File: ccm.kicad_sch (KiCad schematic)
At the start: 22 parts, among them J1 Conn_01x04_Socket, J3 Conn_01x04_Socket, J4 Conn_01x04_Socket, J5 Conn_01x04_Socket, J6 Conn_01x02_Socket, J7 Conn_01x02_Socket, U1 Teensy4.1, U2 LM1117DT-1.8, U3 SN65HVD230, U4 SN65HVD230

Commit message: added DIP socket connector for teensy
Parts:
- U1: footprint teensy:Teensy41 -> teensy:CONN_4848-6000-CP_3MM
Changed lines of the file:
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@@
 			)
 		)
-		(property "Footprint" "teensy:Teensy41"
+		(property "Footprint" "teensy:CONN_4848-6000-CP_3MM"
 			(at 72.39 78.74 0)
 			(effects

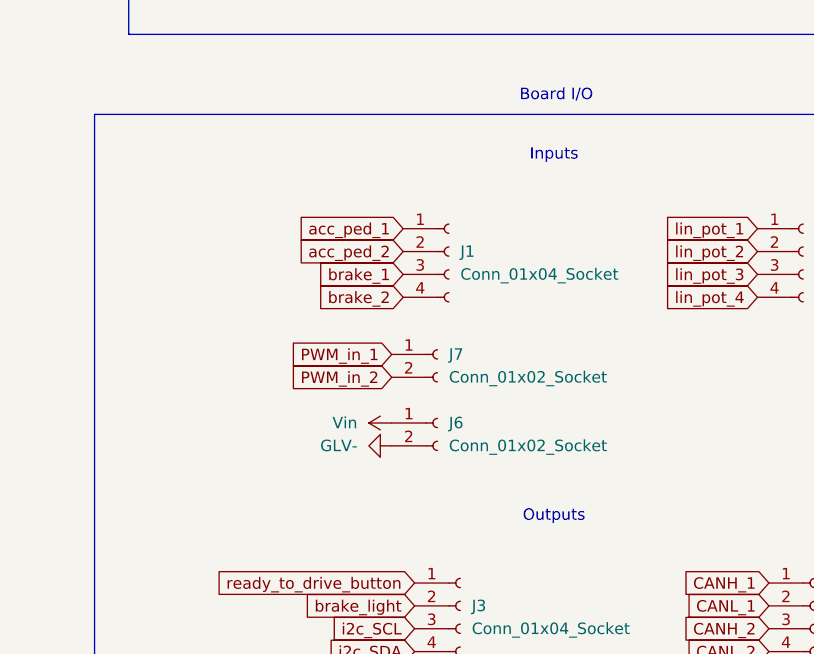
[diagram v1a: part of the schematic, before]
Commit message: change brake and accel connectors
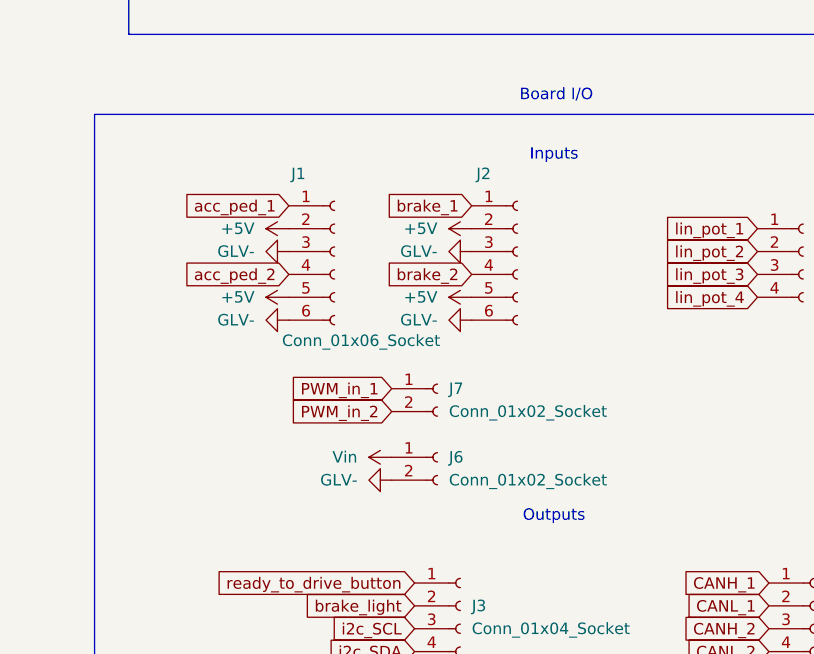
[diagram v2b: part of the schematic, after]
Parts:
- removed J1: Conn_01x04_Socket, Connector_Molex:Molex_Mini-Fit_Jr_5566-04A2_2x02_P4.20mm_Vertical, symbol Connector:Conn_01x04_Socket
- added J1, J2: Conn_01x06_Socket, Connector_Molex:Molex_Mini-Fit_Jr_5566-06A2_2x03_P4.20mm_Vertical, symbol Connector:Conn_01x06_Socket
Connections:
- net +5V: now also J1.2 (Pin_2), J1.5 (Pin_5), J2.2 (Pin_2), J2.5 (Pin_5)
- net GLV-: now also J1.3 (Pin_3), J1.6 (Pin_6), J2.3 (Pin_3), J2.6 (Pin_6)
- net acc_ped_1: now also J1.1 (Pin_1)
- net acc_ped_2: now also J1.4 (Pin_4)
- net brake_1: now also J2.1 (Pin_1)
- net brake_2: now also J2.4 (Pin_4)
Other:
- moved on the sheet: J6, J7

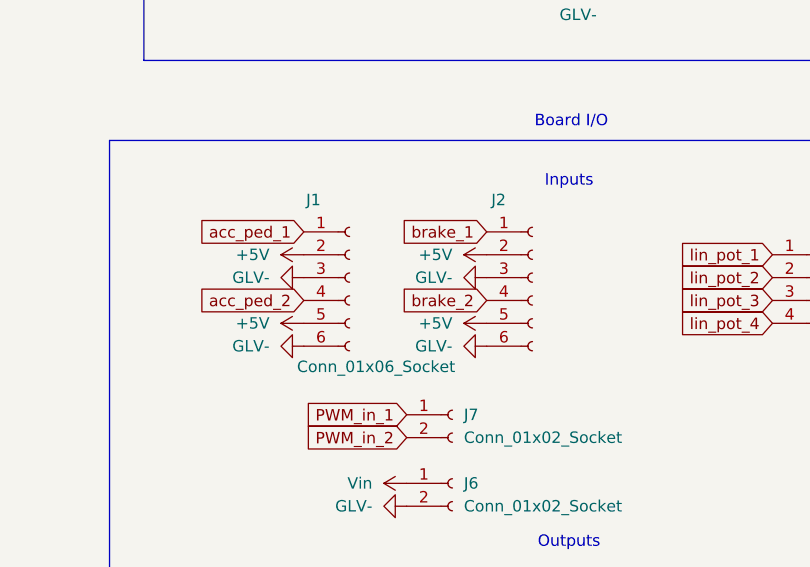
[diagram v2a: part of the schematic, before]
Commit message: remove 5v/glv from throttle/brake sensors
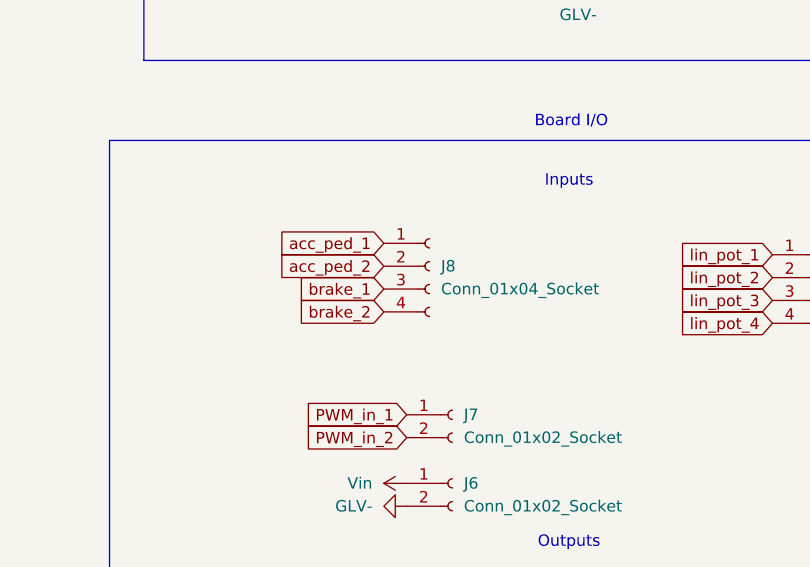
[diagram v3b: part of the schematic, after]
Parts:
- removed J1, J2: Conn_01x06_Socket, Connector_Molex:Molex_Mini-Fit_Jr_5566-06A2_2x03_P4.20mm_Vertical, symbol Connector:Conn_01x06_Socket
- added J8: Conn_01x04_Socket, Connector_Molex:Molex_Mini-Fit_Jr_5566-04A2_2x02_P4.20mm_Vertical, symbol Connector:Conn_01x04_Socket
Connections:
- net acc_ped_1: now also J8.1 (Pin_1)
- net acc_ped_2: now also J8.2 (Pin_2)
- net brake_1: now also J8.3 (Pin_3)
- net brake_2: now also J8.4 (Pin_4)

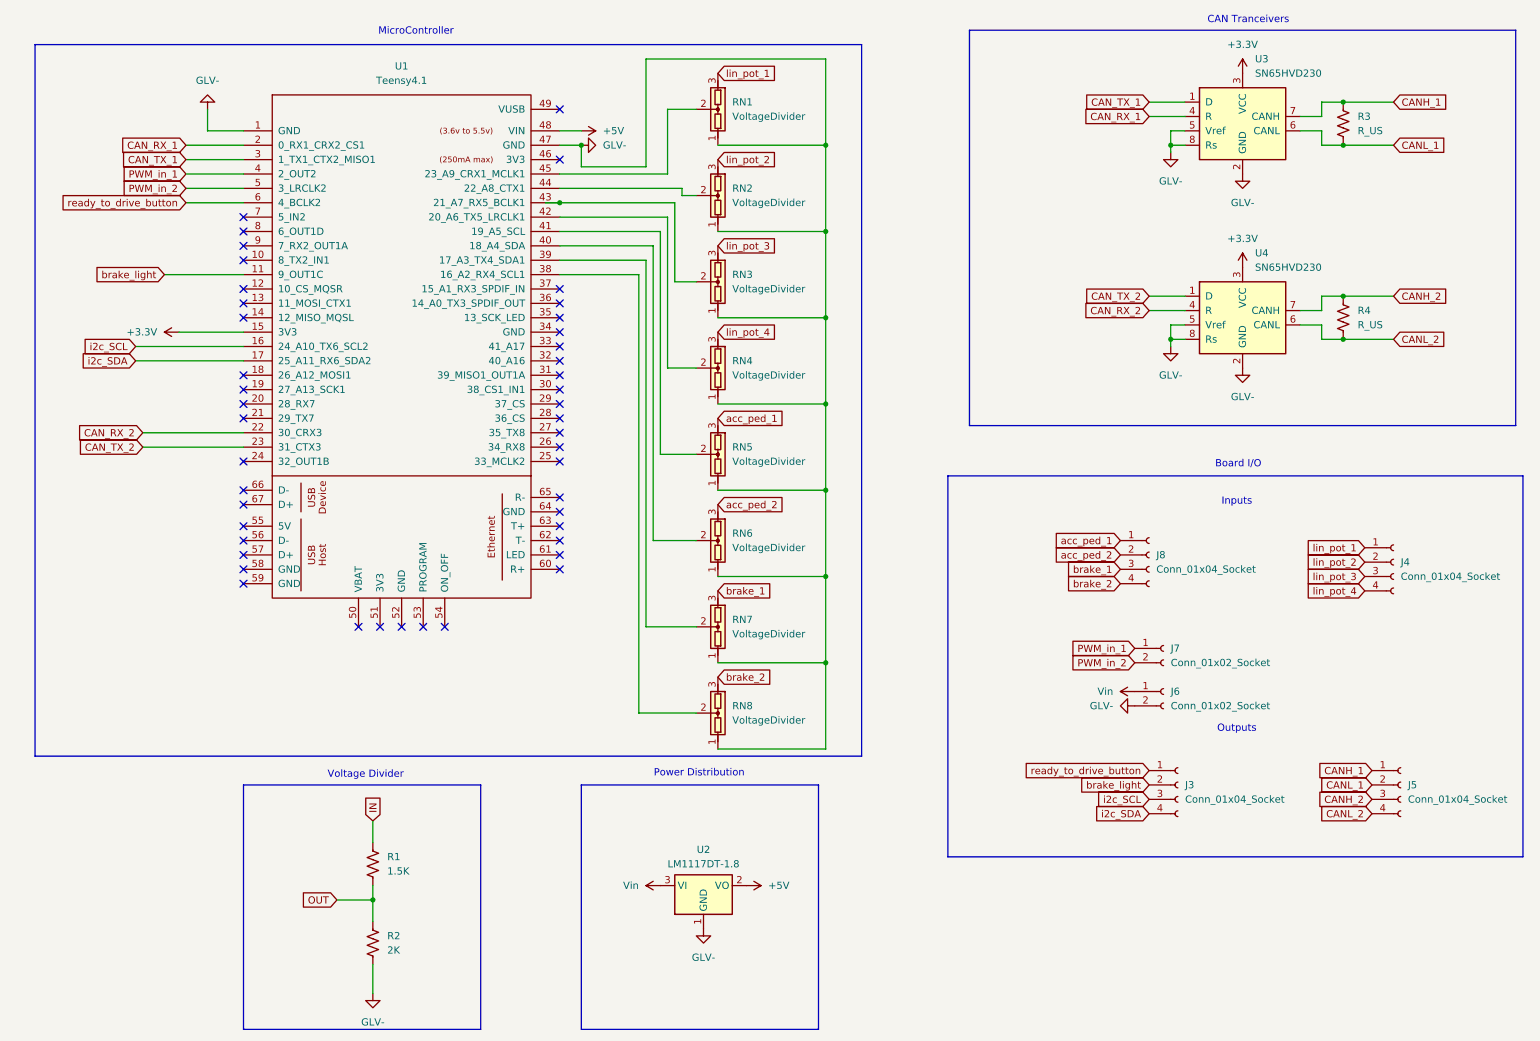
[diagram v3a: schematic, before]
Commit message: add mosfet for brake light output and decoupling capacitors
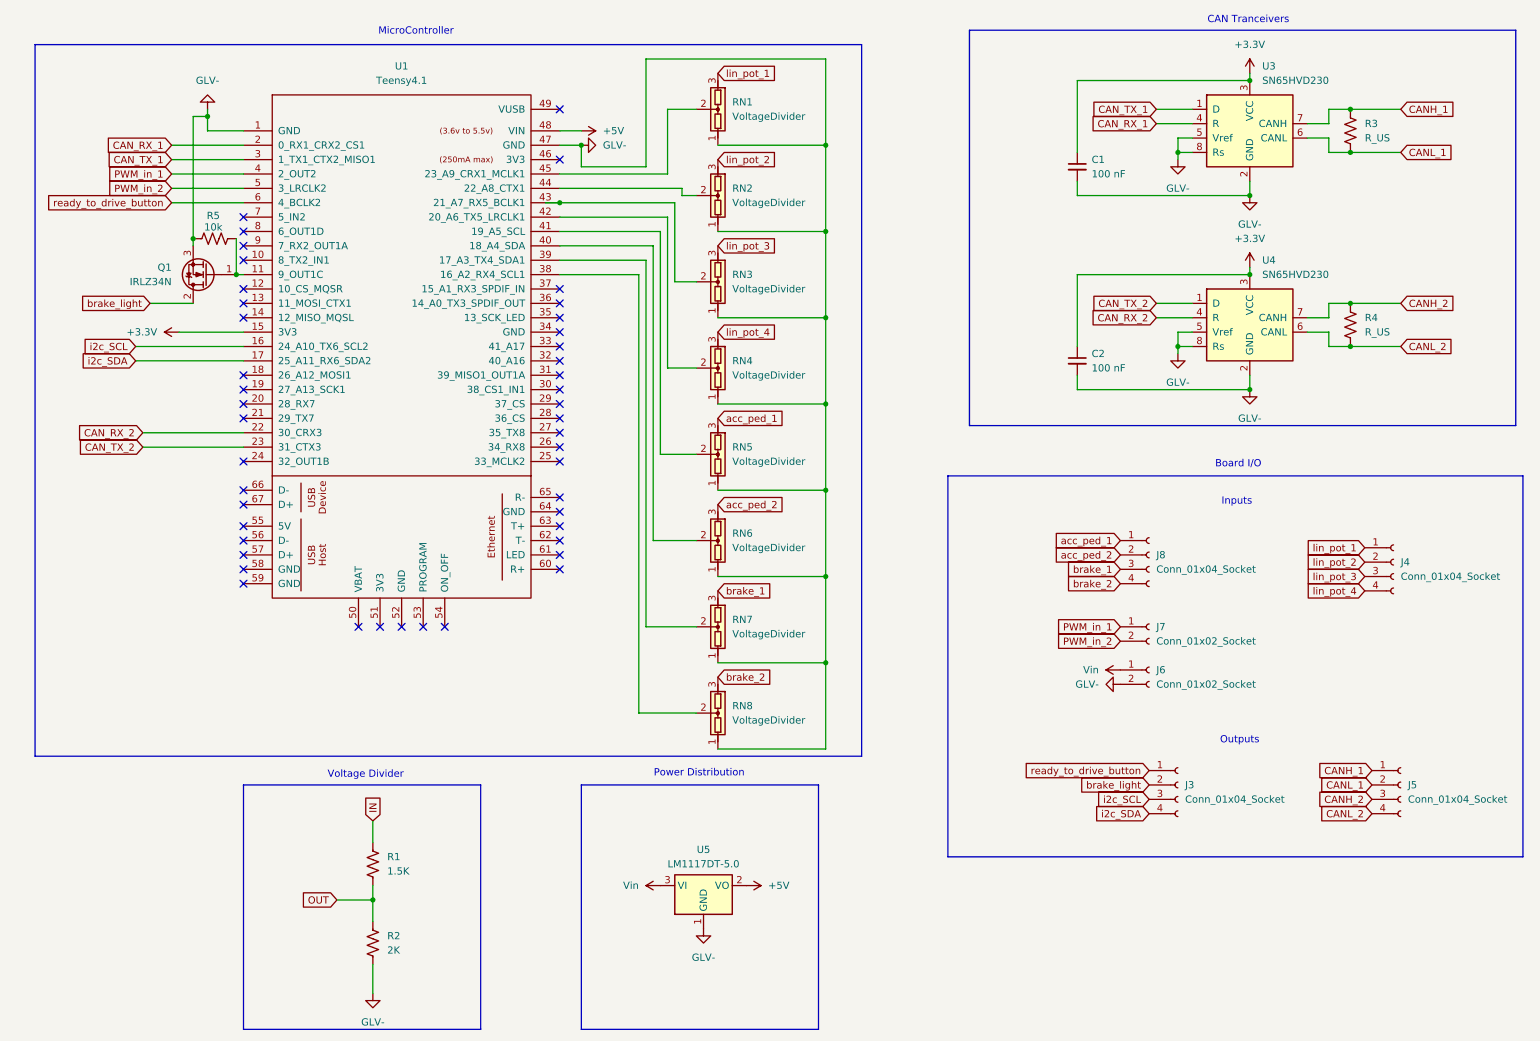
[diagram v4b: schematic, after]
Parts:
- removed U2: LM1117DT-1.8, Package_TO_SOT_SMD:TO-252-3_TabPin2, symbol Regulator_Linear:LM1117DT-1.8
- added C1, C2: 100 nF, Capacitor_SMD:C_0805_2012Metric_Pad1.18x1.45mm_HandSolder, symbol Device:C_Small
- added Q1: IRLZ34N, Package_TO_SOT_THT:TO-220-3_Vertical, symbol Transistor_FET:IRLZ34N
- added R5: 10k, symbol Device:R_US
- added U5: LM1117DT-5.0, Package_TO_SOT_SMD:TO-252-3_TabPin2, symbol Regulator_Linear:LM1117DT-5.0
- R3, R4: footprint Resistor_SMD:R_0805_2012Metric_Pad1.20x1.40mm_HandSolder -> (none)
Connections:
- net +3.3V: now also C1.1, C2.1
- net +5V: now also U5.2 (VO)
- net GLV-: now also C1.2, C2.2, Q1.3 (S), R5.1, U5.1 (GND)
- net Vin: now also U5.3 (VI)
- net brake_light: now also Q1.2 (D); no longer U1.11 (9_OUT1C)
- new net: Q1.1 (G), R5.2, U1.11 (9_OUT1C)
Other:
- moved on the sheet: J6, J7

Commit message: backup commit (no split termination or speaker amp)
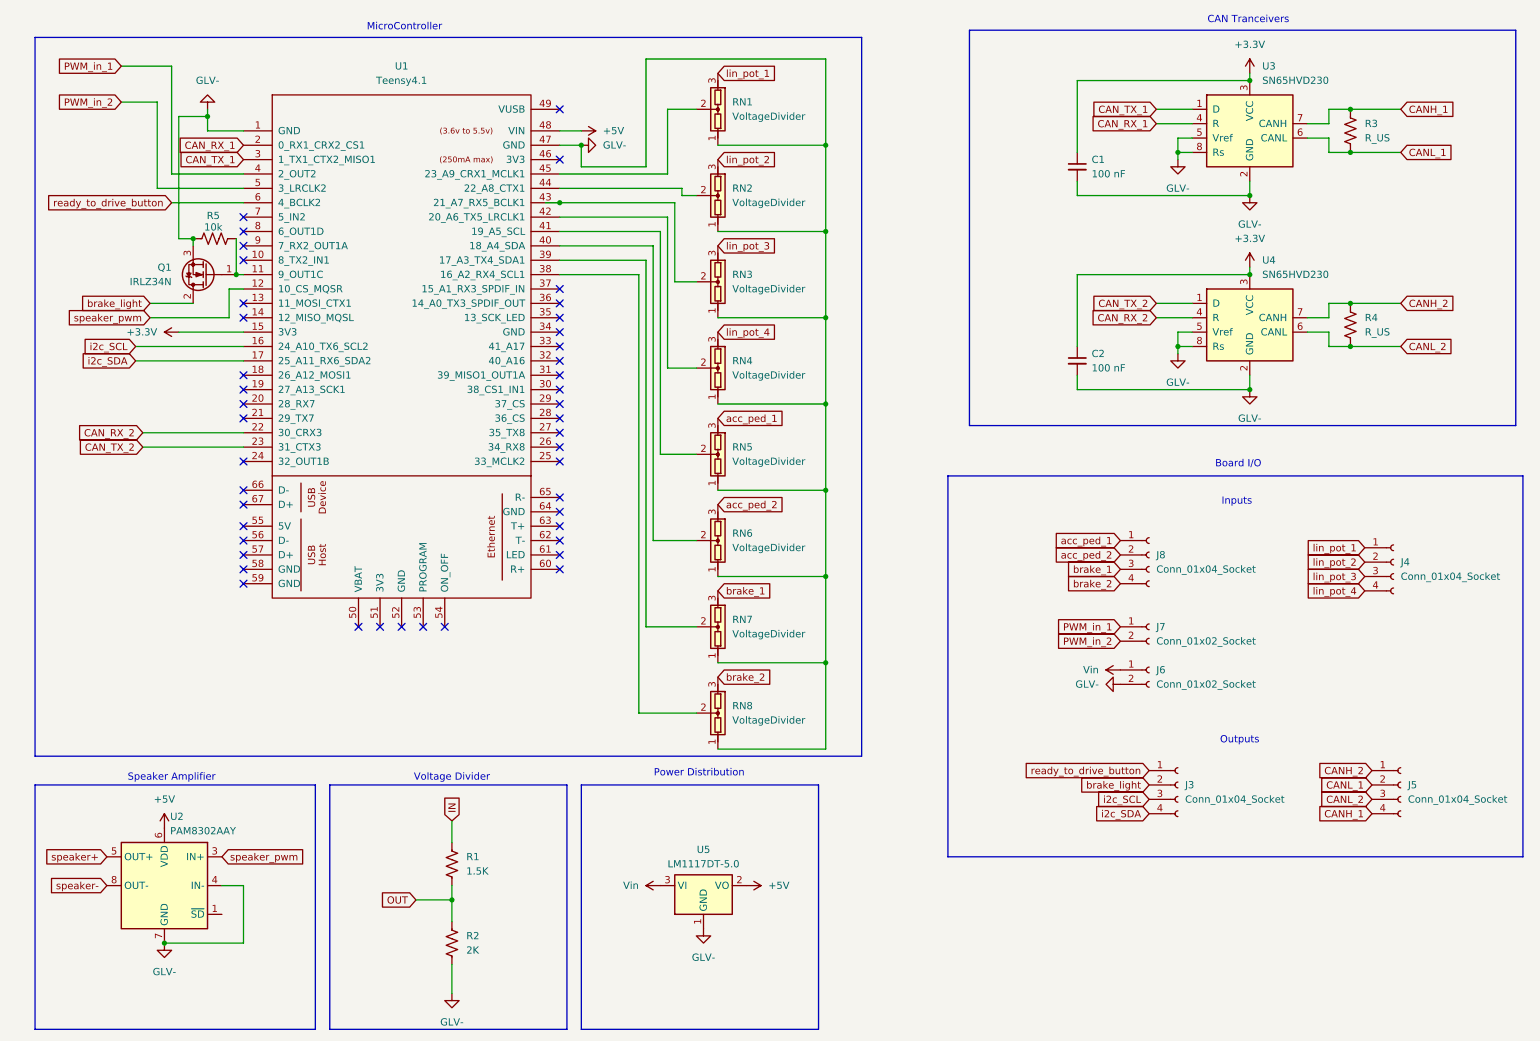
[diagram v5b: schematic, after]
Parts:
- added U2: PAM8302AAY, Package_DFN_QFN:DFN-8-1EP_3x3mm_P0.65mm_EP1.55x2.4mm, symbol Amplifier_Audio:PAM8302AAY
- C1, C2: footprint Capacitor_SMD:C_0805_2012Metric_Pad1.18x1.45mm_HandSolder -> (none)
- R5: footprint (none) -> Resistor_SMD:R_0805_2012Metric_Pad1.20x1.40mm_HandSolder
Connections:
- net +5V: now also U2.6 (VDD)
- net CANH_1: now also J5.4 (Pin_4); no longer J5.1 (Pin_1)
- net CANH_2: now also J5.1 (Pin_1); no longer J5.3 (Pin_3)
- net CANL_2: now also J5.3 (Pin_3); no longer J5.4 (Pin_4)
- net GLV-: now also U2.4 (IN-), U2.7 (GND)
- net speaker_pwm: now reaches U1.12 (10_CS_MQSR)
- net speaker_pwm: now also U2.3 (IN+)
- new net speaker+: U2.5 (OUT+)
- new net speaker-: U2.8 (OUT-)
- no-connect marks 45 -> 44
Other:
- note added: "Speaker Amplifier"
- moved on the sheet: R1, R2
